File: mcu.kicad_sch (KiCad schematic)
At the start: 11 parts, among them J3 Teensy_UART, J3 USB_C_Receptacle_USB2.0, J4 UnusedPins_1, J5 I2C0, J6 I2C1, J8 UnusedPins_2, U1 Teensy4.0

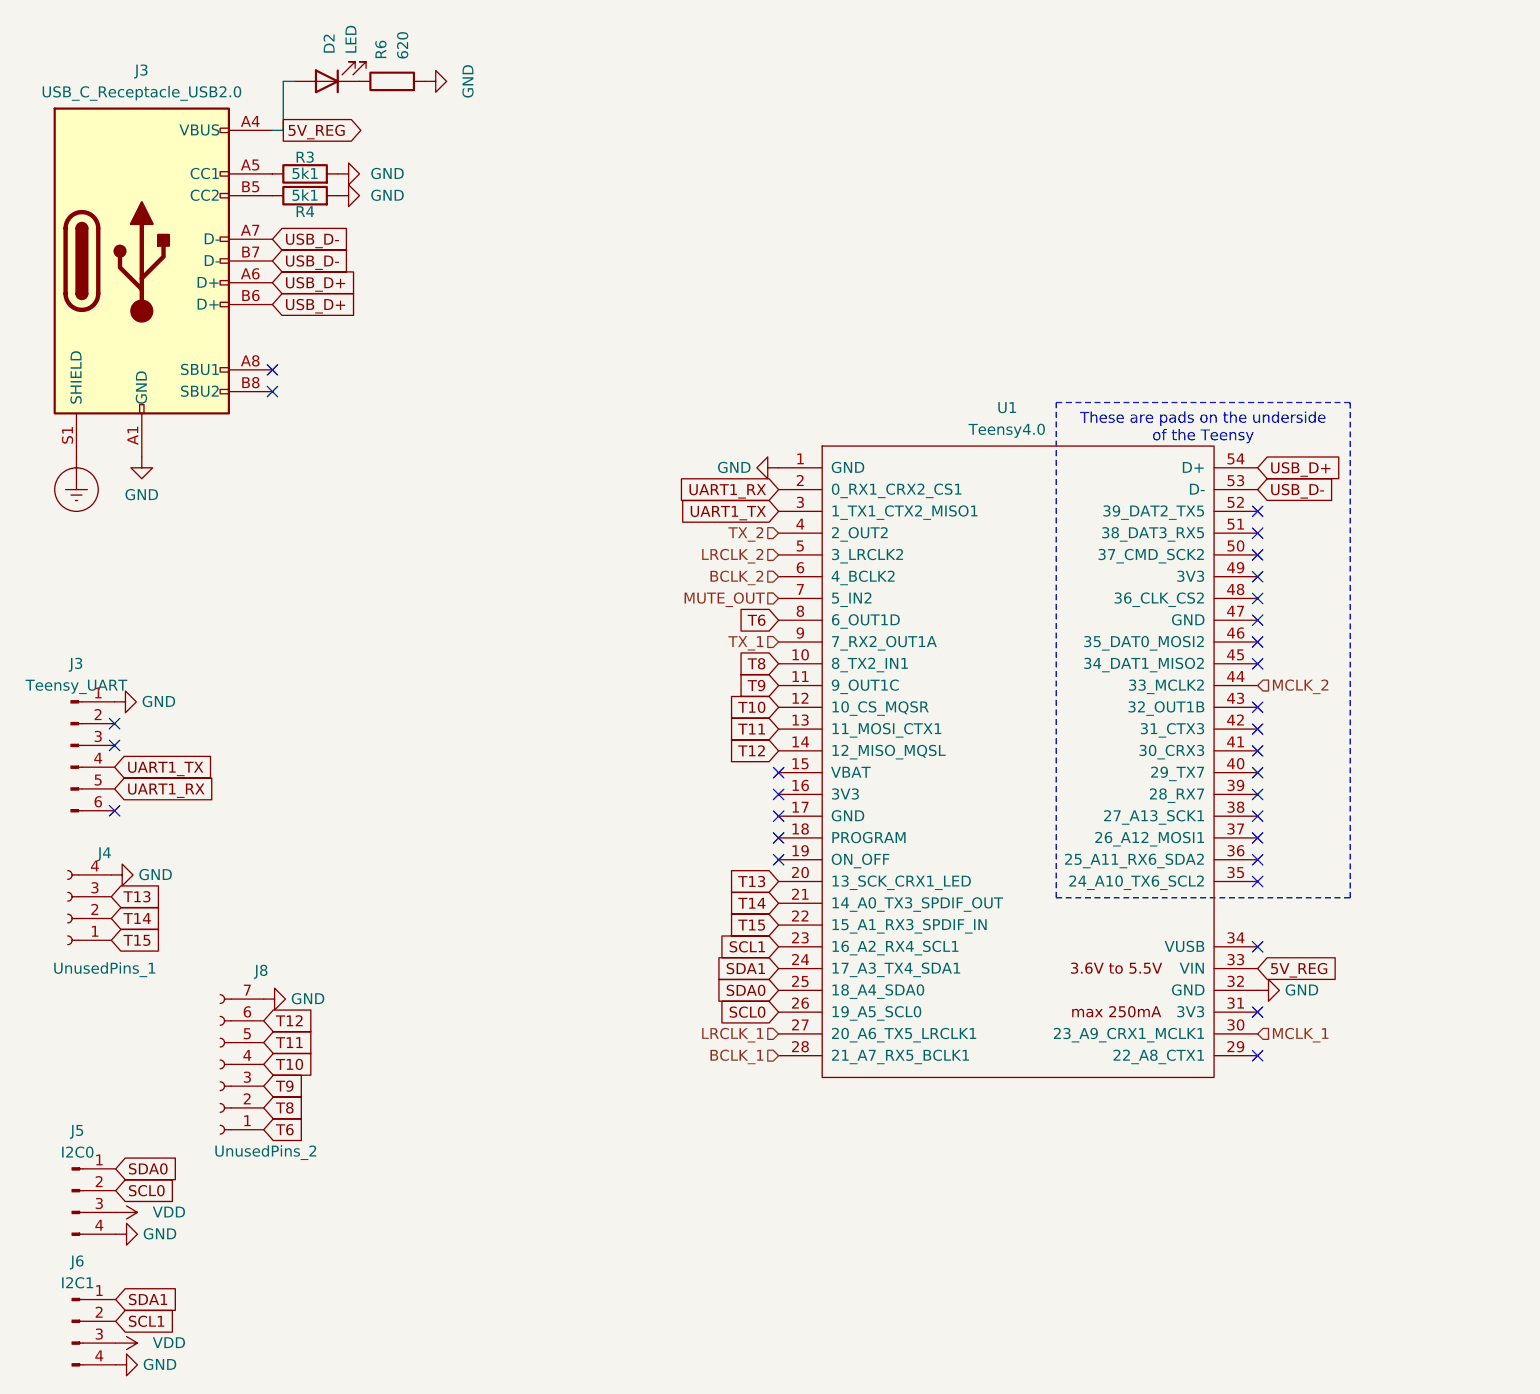
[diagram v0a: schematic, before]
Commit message: Removed USB-C port, see issue #1
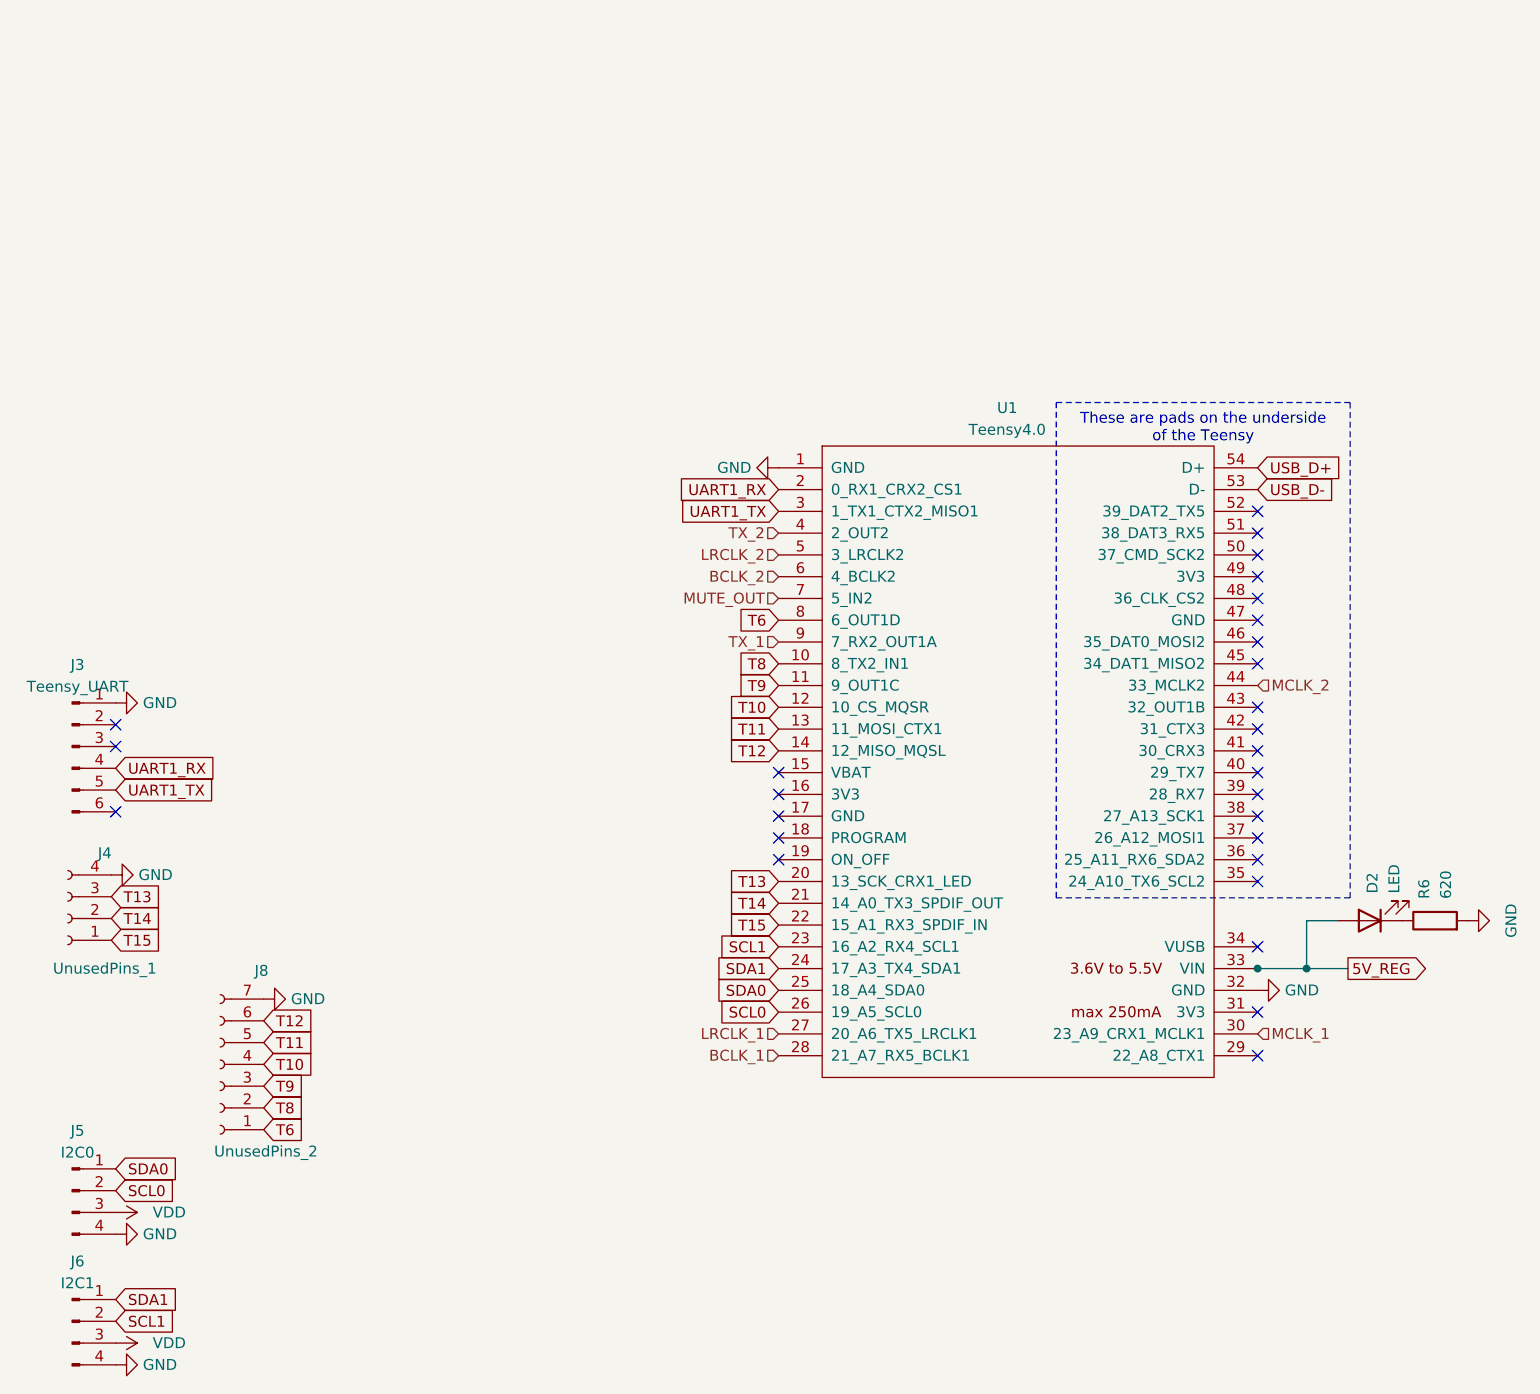
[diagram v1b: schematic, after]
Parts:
- removed J3: USB_C_Receptacle_USB2.0, Connector_USB:USB_C_Receptacle_HRO_TYPE-C-31-M-12, symbol Connector:USB_C_Receptacle_USB2.0
- removed R3, R4: 5k1, Resistor_SMD:R_0805_2012Metric_Pad1.20x1.40mm_HandSolder, symbol Device:R
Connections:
- net UART1_RX: now also J3.4 (Pin_4); no longer J3.5 (Pin_5)
- net UART1_TX: now also J3.5 (Pin_5); no longer J3.4 (Pin_4)
- no-connect marks 30 -> 28
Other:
- moved on the sheet: D2, R6
